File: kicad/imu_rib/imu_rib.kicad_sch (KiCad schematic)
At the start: 6 parts, among them J1 Conn_01x06_Pin, U1 LSM9DS1

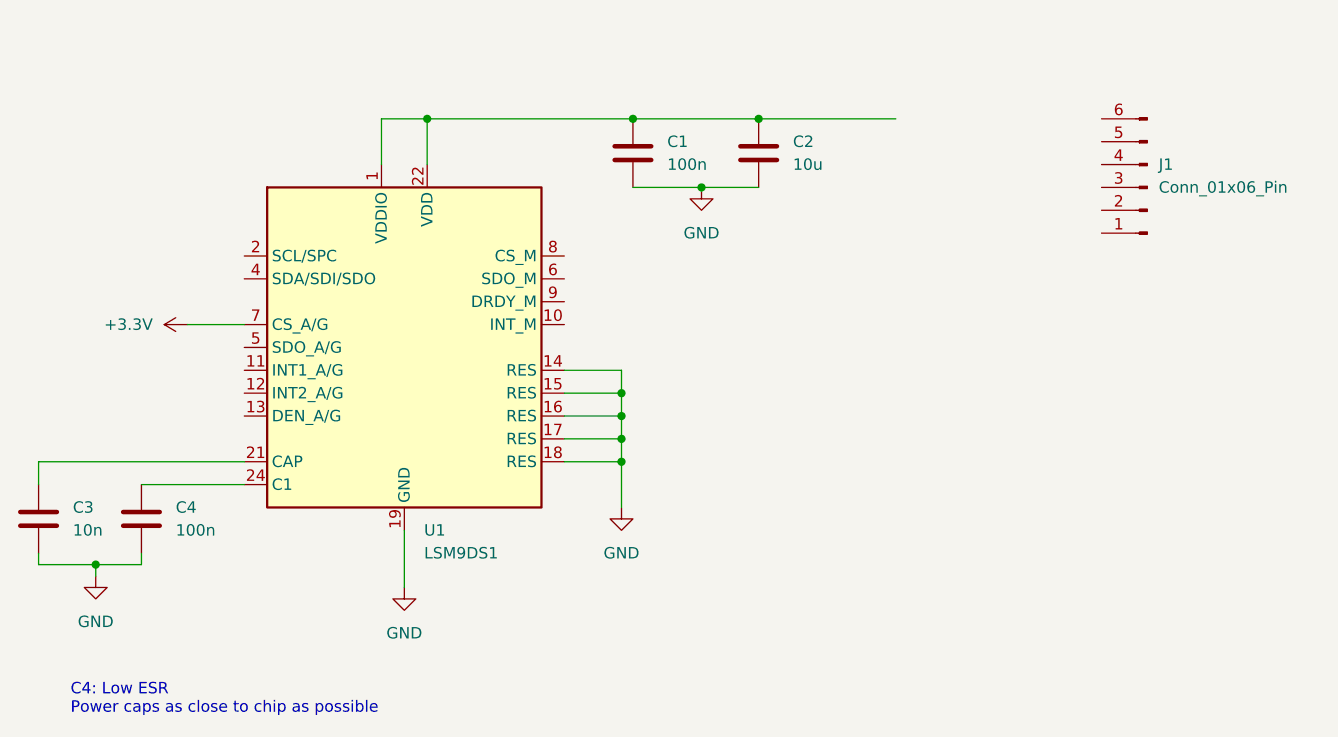
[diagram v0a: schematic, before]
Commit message: update imu rib schematic with i2c wires
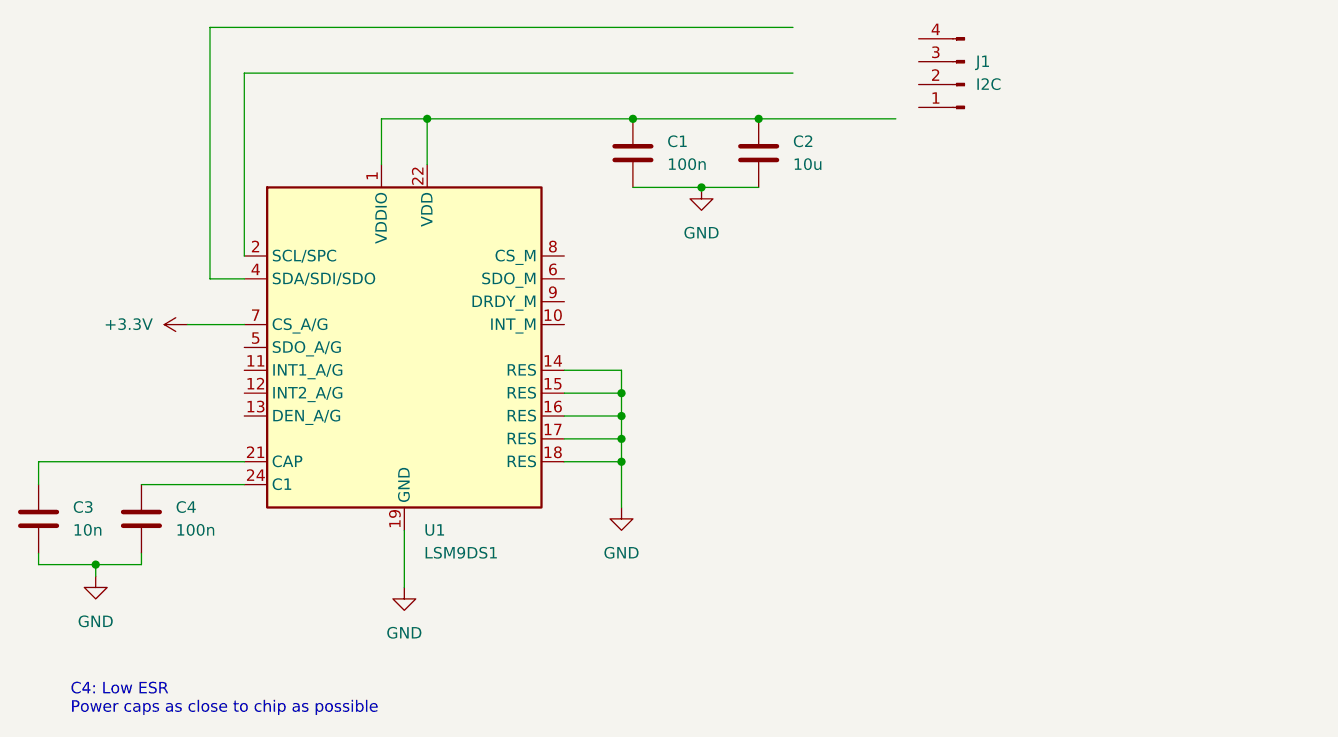
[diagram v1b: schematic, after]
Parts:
- removed J1: Conn_01x06_Pin, symbol Connector:Conn_01x06_Pin
- added J1: I2C, symbol Connector:Conn_01x04_Pin
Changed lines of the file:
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@@
+	(wire
+		(pts
+			(xy 96.52 41.91) (xy 157.48 41.91)
+		)
+		(stroke
+			(width 0)
+			(type default)
+		)
+	)
 	(wire
 		(pts
@@
 	(wire
 		(pts
+			(xy 96.52 64.77) (xy 92.71 64.77)
+		)
+		(stroke
+			(width 0)
+			(type default)
+		)
+	)
+	(wire
+		(pts
 			(xy 153.67 46.99) (xy 168.91 46.99)
 		)
@@
 	(wire
 		(pts
+			(xy 96.52 62.23) (xy 96.52 41.91)
+		)
+		(stroke
+			(width 0)
+			(type default)
+		)
+	)
+	(wire
+		(pts
 			(xy 132.08 80.01) (xy 138.43 80.01)
 		)
@@
 	(wire
 		(pts
+			(xy 92.71 36.83) (xy 157.48 36.83)
+		)
+		(stroke
+			(width 0)
+			(type default)
+		)
+	)
+	(wire
+		(pts
 			(xy 138.43 90.17) (xy 138.43 85.09)
+		)
+		(stroke
+			(width 0)
+			(type default)
+		)
+	)
+	(wire
+		(pts
+			(xy 92.71 64.77) (xy 92.71 36.83)
 		)
 		(stroke
@@
 	)
 	(symbol
+		(lib_id "Connector:Conn_01x04_Pin")
+		(at 176.53 43.18 180)
+		(unit 1)
+		(exclude_from_sim no)
+		(in_bom yes)
+		(on_board yes)
+		(dnp no)
+		(fields_autoplaced yes)
+		(property "Reference" "J1"
+			(at 177.8 40.6399 0)
+			(effects
+				(font
+					(size 1.27 1.27)
+				)
+				(justify right)
+			)
+		)
+		(property "Value" "I2C"
+			(at 177.8 43.1799 0)
+			(effects
+				(font
+					(size 1.27 1.27)
+				)
+				(justify right)
+			)
+		)
+		(property "Footprint" ""
+			(at 176.53 43.18 0)
+			(effects
+				(font
+					(size 1.27 1.27)
+				)
+				(hide yes)
+			)
+		)
+		(property "Datasheet" "~"
+			(at 176.53 43.18 0)
+			(effects
+				(font
+					(size 1.27 1.27)
+				)
+				(hide yes)
+			)
+		)
+		(property "Description" "Generic connector, single row, 01x04, script generated"
+			(at 176.53 43.18 0)
+			(effects
+				(font
+					(size 1.27 1.27)
+				)
+				(hide yes)
+			)
+		)
+		(pin "1"
+		)
+		(pin "2"
+		)
+		(pin "4"
+		)
+		(pin "3"
+		)
+		(instances
+			(project ""
+				(path "/ab36c0e3-095d-4714-830b-404fd8916e01"
+					(reference "J1")
+					(unit 1)
+				)
+			)
+		)
+	)
+	(symbol
 		(lib_id "power:+3.3V")
 		(at 90.17 69.85 90)
@@
 					(unit 1)
 				)
-			)
-		)
-	)
-	(symbol
-		(lib_id "Connector:Conn_01x06_Pin")
-		(at 196.85 54.61 180)
-		(unit 1)
-		(exclude_from_sim no)
-		(in_bom yes)
-		(on_board yes)
-		(dnp no)
-		(fields_autoplaced yes)
-		(property "Reference" "J1"
-			(at 198.12 52.0699 0)
-			(effects
-				(font
-					(size 1.27 1.27)
-				)
-				(justify right)
-			)
-		)
-		(property "Value" "Conn_01x06_Pin"
-			(at 198.12 54.6099 0)
-			(effects
-				(font
-					(size 1.27 1.27)
-				)
-				(justify right)
-			)
-		)
-		(property "Footprint" ""
-			(at 196.85 54.61 0)
-			(effects
-				(font
-					(size 1.27 1.27)
-				)
-				(hide yes)
-			)
-		)
-		(property "Datasheet" "~"
-			(at 196.85 54.61 0)
-			(effects
-				(font
-					(size 1.27 1.27)
-				)
-				(hide yes)
-			)
-		)
-		(property "Description" "Generic connector, single row, 01x06, script generated"
-			(at 196.85 54.61 0)
-			(effects
-				(font
-					(size 1.27 1.27)
-				)
-				(hide yes)
-			)
-		)
-		(pin "2"
-		)
-		(pin "6"
-		)
-		(pin "4"
-		)
-		(pin "3"
-		)
-		(pin "5"
-		)
-		(pin "1"
-		)
-		(instances
-			(project ""
-				(path "/ab36c0e3-095d-4714-830b-404fd8916e01"
-					(reference "J1")
-					(unit 1)
-				)
